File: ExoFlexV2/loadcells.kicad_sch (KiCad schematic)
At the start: 7 parts

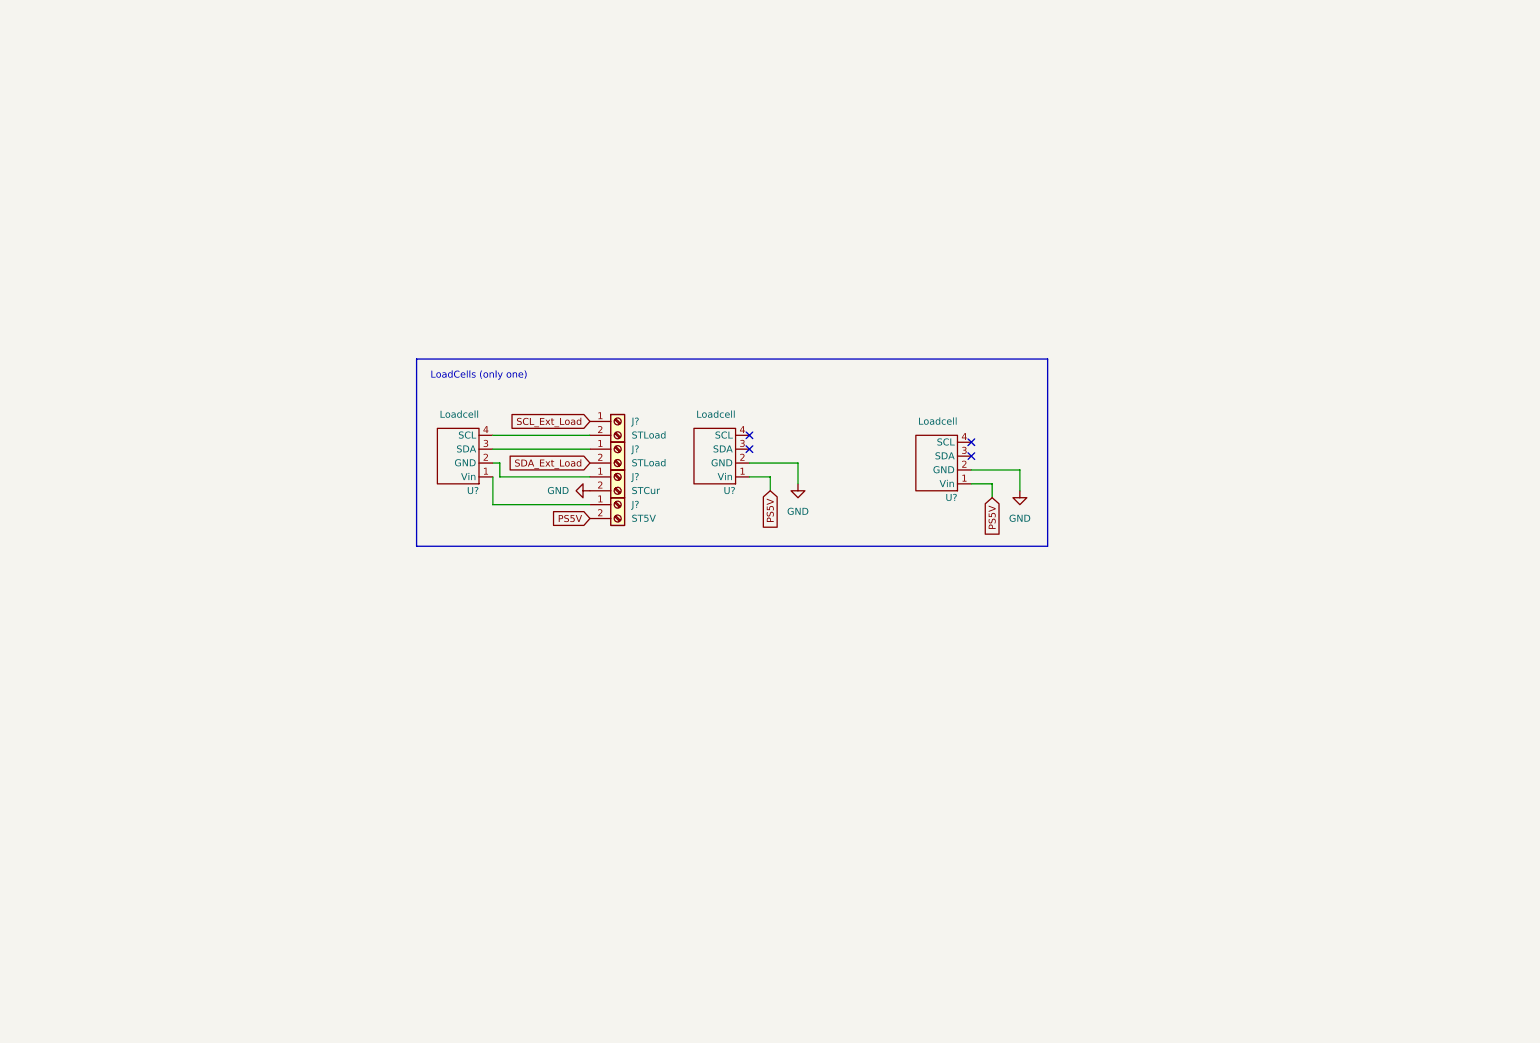
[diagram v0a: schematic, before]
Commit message: Schematic structure
Ajout des Encodeur magnétique et load cells, début de circuit de comparateurs
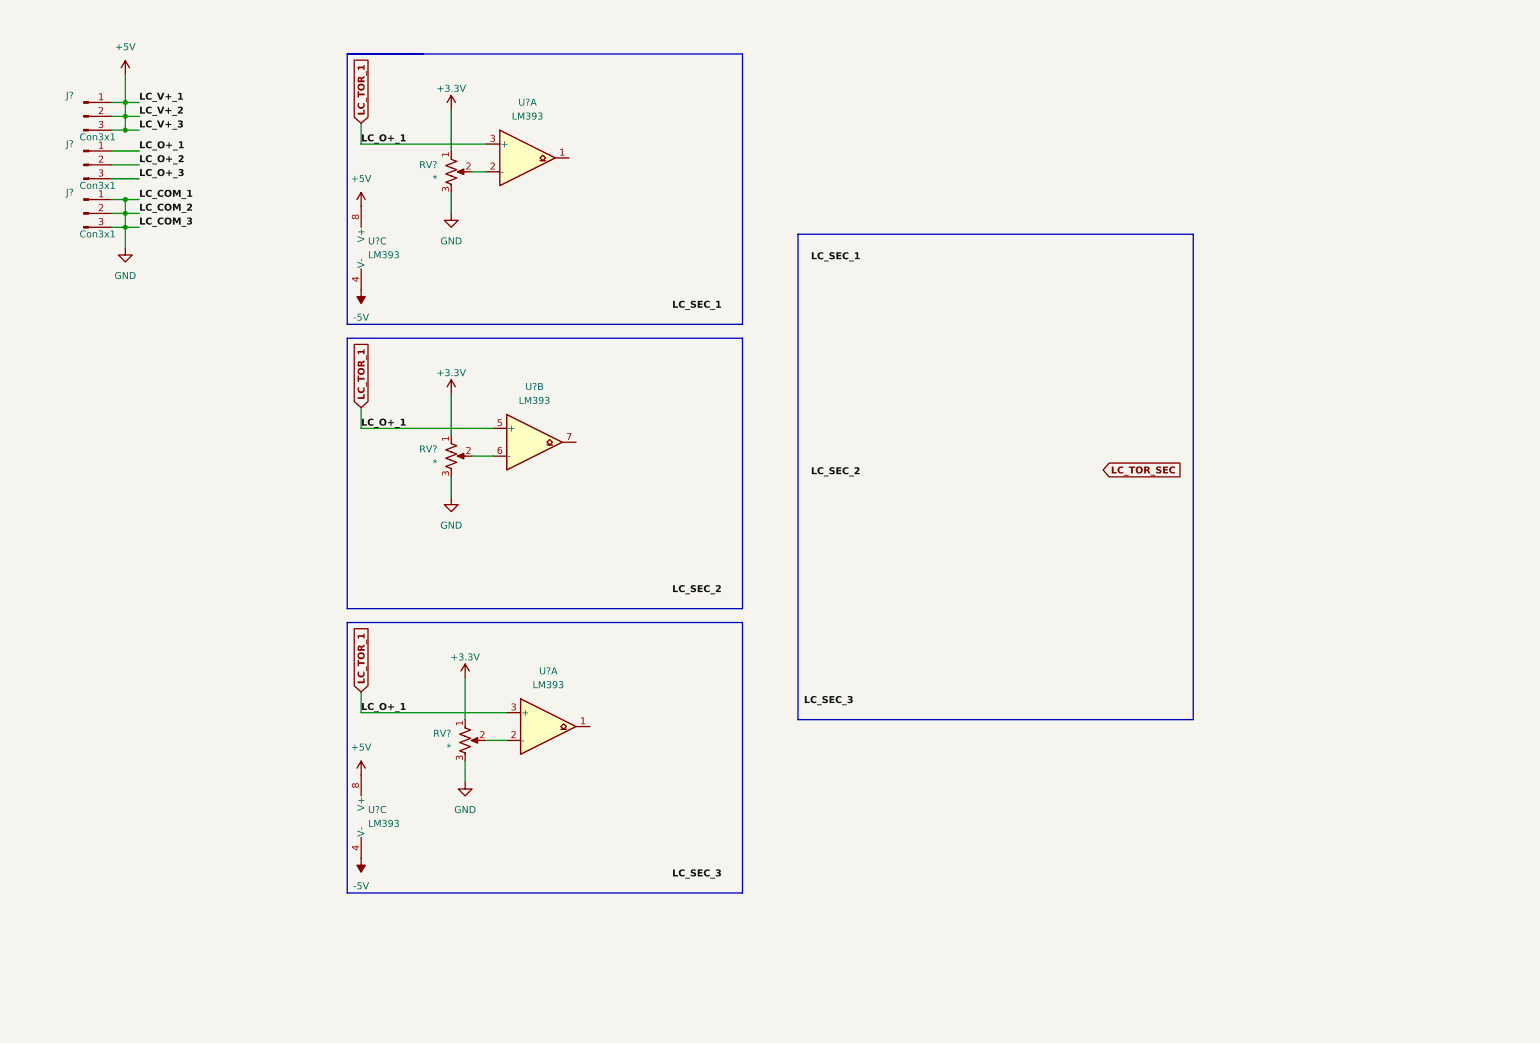
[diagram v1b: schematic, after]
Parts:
- removed J? (x2): STLoad, symbol Connector:Screw_Terminal_01x02
- removed J?: STCur, symbol Connector:Screw_Terminal_01x02
- removed J?: ST5V, symbol Connector:Screw_Terminal_01x02
- removed U? (x3): Loadcell, symbol Sensor_library:MPU6050_acc_gyro
- added J? (x3): Con3x1, symbol Connector:Conn_01x03_Male
- added RV? (x3): *, symbol Device:R_Potentiometer_US
- added U? (x5): LM393, symbol Comparator:LM393
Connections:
- net GND: now also J?.1 (Pin_1), J?.2 (Pin_2), J?.3 (Pin_3), RV?.3, RV?.3, RV?.3
- new net: RV?.2, U?.2 (-) (x2)
- new net: RV?.2, U?.6 (-)
- new net +3.3V: RV?.1, RV?.1, RV?.1
- new net +5V: J?.1 (Pin_1), J?.2 (Pin_2), J?.3 (Pin_3), U?.8 (V+), U?.8 (V+)
- new net -5V: U?.4 (V-), U?.4 (V-)
- new net LC_O+_2: J?.2 (Pin_2)
- new net LC_O+_3: J?.3 (Pin_3)
- new net LC_TOR_1: J?.1 (Pin_1), U?.3 (+), U?.3 (+), U?.5 (+)
- no-connect marks 4 -> 0
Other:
- note removed: "LoadCells (only one)"

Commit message: Many changes
Debouncing, power protection, potentiometer limits, etc.
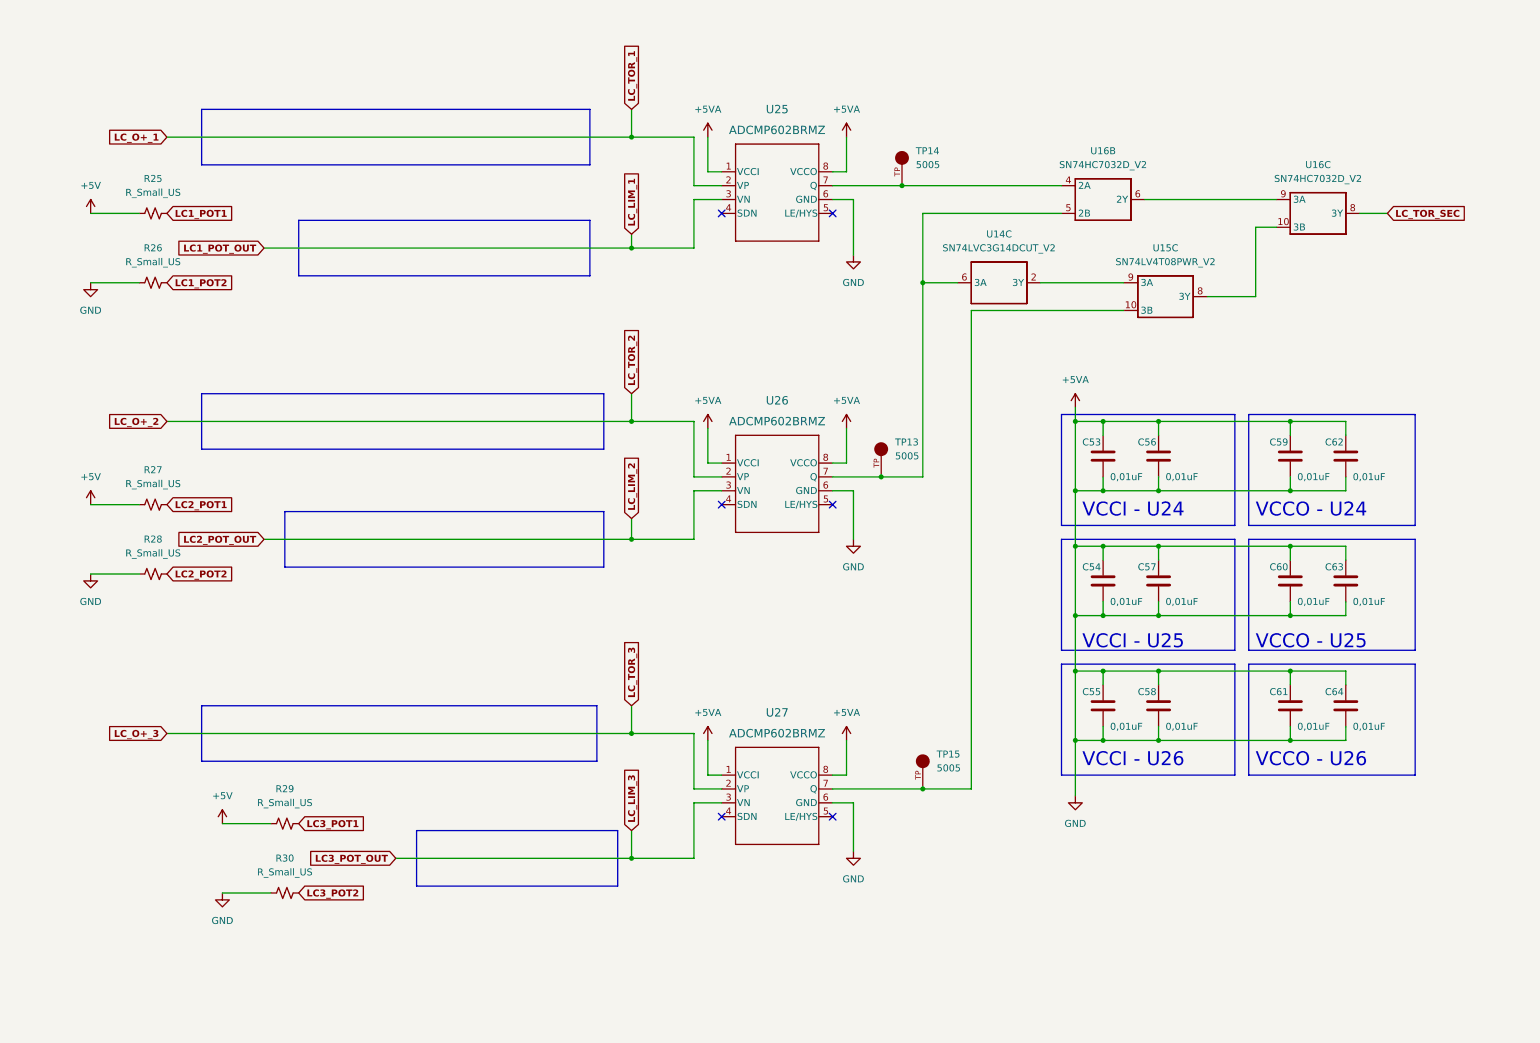
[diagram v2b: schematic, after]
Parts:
- removed J? (x3): Con3x1, symbol Connector:Conn_01x03_Male
- removed RV? (x3): *, symbol Device:R_Potentiometer_US
- removed U? (x5): LM393, symbol Comparator:LM393
- added C53, C54, C55, C56, C57, C58, C59, C60, C61, C62, C63, C64: 0,01uF, Capacitor_SMD:C_0603_1608Metric, symbol Device:C
- added R25, R26, R27, R28, R29, R30: R_Small_US, Resistor_SMD:R_0603_1608Metric, symbol Device:R_Small_US
- added TP13, TP14, TP15: 5005, FootPrint:KEYSTONE_5005, symbol SymLib:5005
- added U14: SN74LVC3G14DCUT_V2, FootPrint:SN74LVC3G14DCUT, symbol SymLib:SN74LVC3G14DCUT_V2
- added U15: SN74LV4T08PWR_V2, FootPrint:SN74LV4T08PWR, symbol SymLib:SN74LV4T08PWR_V2
- added U16: SN74HC7032D_V2, FootPrint:SN74HC7032D, symbol SymLib:SN74HC7032D_V2
- added U25, U26, U27: ADCMP602BRMZ, FootPrint:ADCMP602BRMZ, symbol SymLib:ADCMP602BRMZ
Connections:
- net +5V: now also R25.1, R27.1, R29.1
- net LC_O+_2: now also U26.2 (VP)
- net LC_O+_3: now also U27.2 (VP)
- net LC_TOR_SEC: now also U16.8 (3Y)
- new net: TP13.TP, U14.6 (3A), U16.5 (2B), U26.7 (Q)
- new net: TP15.TP, U15.10 (3B), U27.7 (Q)
- new net: U14.2 (3Y), U15.9 (3A)
- new net: TP14.TP, U16.4 (2A), U25.7 (Q)
- new net: U15.8 (3Y), U16.10 (3B)
- new net: U16.6 (2Y), U16.9 (3A)
- new net +5VA: C53.1, C53.2, C54.1, C54.2, C55.1, C55.2, C56.1, C56.2, C57.1, C57.2, C58.1, C58.2, C59.1, C59.2, C60.1, C60.2, C61.1, C61.2, C62.1, C62.2, C63.1, C63.2, C64.1, C64.2, R26.1, R28.1, R30.1, U25.1 (VCCI), U25.6 (GND), U25.8 (VCCO), U26.1 (VCCI), U26.6 (GND), U26.8 (VCCO), U27.1 (VCCI), U27.6 (GND), U27.8 (VCCO)
- new net LC1_POT1: R25.2
- new net LC1_POT2: R26.2
- new net LC1_POT_OUT: U25.3 (VN)
- new net LC2_POT1: R27.2
- new net LC2_POT2: R28.2
- new net LC2_POT_OUT: U26.3 (VN)
- new net LC3_POT1: R29.2
- new net LC3_POT2: R30.2
- new net LC3_POT_OUT: U27.3 (VN)
- new net LC_O+_1: U25.2 (VP)
- no-connect marks 0 -> 6
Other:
- note added: "VCCI - U24"
- note added: "VCCI - U25"
- note added: "VCCI - U26"
- note added: "VCCO - U24"
- note added: "VCCO - U25"
- note added: "VCCO - U26"

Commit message: quque truc
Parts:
- added C62, C63, C64, C65, C66, C70: 1nF, Capacitor_SMD:C_0603_1608Metric, symbol Device:C
- added C67, C68, C69: 0,1uF, Capacitor_SMD:C_0603_1608Metric, symbol Device:C
- added C71, C72, C73: 1uF, Capacitor_SMD:C_0603_1608Metric, symbol Device:C
- added R42, R43, R46, R47, R48, R52: 7,5k, Resistor_SMD:R_0603_1608Metric, symbol Device:R_Small_US
- added R49, R50, R51: 10k, Resistor_SMD:R_0603_1608Metric, symbol Device:R_Small_US
- added R53, R54, R55: 220k, Resistor_SMD:R_0603_1608Metric, symbol Device:R_Small_US
- added R56, R57, R58, R62, R63, R64: 2M, Resistor_SMD:R_0603_1608Metric, symbol Device:R_Small_US
- added R59, R60, R61: 430k, Resistor_SMD:R_0603_1608Metric, symbol Device:R_Small_US
- added TP32, TP33, TP34, TP35, TP36, TP37, TP41: 5005, FootPrint:KEYSTONE_5005, symbol SymLib:5005
- added U24, U25, U26: MCP6001T-I_OT, FootPrint:SOT95P270X145-5N, symbol SymLib:MCP6001T-I_OT
- renumbered C53 to C74, C54 to C75, C55 to C76, C56 to C77, C57 to C78, C58 to C79, C59 to C80, C60 to C81, C61 to C82, C62 to C83, C63 to C84, C64 to C85, R25 to R38, R26 to R39, R27 to R40, R28 to R41, R29 to R44, R30 to R45, TP13 to TP38, TP14 to TP39, TP15 to TP40, U14 to U15, U15 to U16, U16 to U17, U25 to U27, U26 to U28, U27 to U29
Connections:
- net +5V is gone; now on net +5VA: R38.1, R40.1, R44.1
- net +5VA: now also C67.1, C68.1, C69.1, C71.1, C72.1, C73.1, U24.5, U25.5, U26.5; no longer C74.2, C75.2, C76.2, C77.2, C78.2, C79.2, C80.2, C81.2, C82.2, C83.2, C84.2, C85.2, R39.1, R41.1, R45.1, U27.6 (GND), U28.6 (GND), U29.6 (GND)
- net LC1_POT_OUT: now also R46.1; no longer U27.3 (VN)
- net LC2_POT_OUT: now also R48.1; no longer U28.3 (VN)
- net LC3_POT_OUT: now also R52.1; no longer U29.3 (VN)
- net LC_O+_1: now also R47.1; no longer U27.2 (VP)
- net LC_O+_2: now also R43.1; no longer U28.2 (VP)
- net LC_O+_3: now also R42.1; no longer U29.2 (VP)
- net LC_TOR_SEC: now also TP41.TP
- new net: C64.1, R47.2, U24.3
- new net: R49.2, R53.1, R56.1, U24.4
- new net: R56.2, R59.2, R62.1
- new net: C62.1, R42.2, U26.3
- new net: C63.1, R43.2, U25.3
- new net: R53.2, R59.1
- new net: R51.2, R55.1, R58.1, U26.4
- new net: R58.2, R61.2, R64.1
- new net: R50.2, R54.1, R57.1, U25.4
- new net: R55.2, R61.1
- new net: R54.2, R60.1
- new net: R57.2, R60.2, R63.1
- new net GND: C62.2, C63.2, C64.2, C65.2, C66.2, C67.2, C68.2, C69.2, C70.2, C71.2, C72.2, C73.2, C74.2, C75.2, C76.2, C77.2, C78.2, C79.2, C80.2, C81.2, C82.2, C83.2, C84.2, C85.2, R39.1, R41.1, R45.1, R49.1, R50.1, R51.1, U24.2, U25.2, U26.2, U27.6 (GND), U28.6 (GND), U29.6 (GND)
- new net LC_LIM_1: C65.1, R46.2, TP33.TP, U27.3 (VN)
- new net LC_LIM_2: C66.1, R48.2, TP35.TP, U28.3 (VN)
- new net LC_LIM_3: C70.1, R52.2, TP37.TP, U29.3 (VN)
- new net LC_TOR_1: R62.2, TP32.TP, U24.1, U27.2 (VP)
- new net LC_TOR_2: R63.2, TP34.TP, U25.1, U28.2 (VP)
- new net LC_TOR_3: R64.2, TP36.TP, U26.1, U29.2 (VP)
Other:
- moved on the sheet: R38, R39, R40, R41, R44, R45

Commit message: Placement
Début du placement et modification d'après dernier review
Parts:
- added TP69, TP70, TP71: 5005, FootPrint:KEYSTONE_5005, symbol SymLib:5005
- R37: renamed from R38; value R_Small_US -> 0Ω
- R38: renamed from R39; value R_Small_US -> 0Ω
- R39: renamed from R40; value R_Small_US -> 0Ω
- R40: renamed from R41; value R_Small_US -> 0Ω
- R42: renamed from R44; value R_Small_US -> 0Ω
- R43: renamed from R45; value R_Small_US -> 0Ω
- renumbered C64 to C66, C65 to C67, C63 to C68, C66 to C69, C62 to C70, C67 to C71, C68 to C72, C69 to C73, C71 to C74, C72 to C75, C73 to C76, C70 to C77, C74 to C78, C75 to C79, C76 to C80, C77 to C81, C78 to C82, C79 to C83, C80 to C84, C81 to C85, C82 to C86, C83 to C87, C84 to C88, C85 to C89, R48 to R41, R46 to R44, R43 to R45, R47 to R46, R42 to R47, R49 to R48, R50 to R49, R51 to R50, R53 to R51, R54 to R52, R55 to R53, R56 to R54, R57 to R55, R58 to R56, R59 to R57, R60 to R58, R61 to R59, R52 to R60, R62 to R61, R63 to R62, R64 to R63, TP32 to TP60, TP33 to TP61, TP34 to TP62, TP35 to TP63, TP36 to TP64, TP37 to TP65, TP38 to TP66, TP39 to TP67, TP40 to TP68, TP41 to TP72, U15 to U13, U16 to U15, U17 to U16
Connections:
- net at U13.2 (3Y), U15.9 (3A): now also TP69.TP
- net at U15.8 (3Y), U16.10 (3B): now also TP71.TP
- net at U16.6 (2Y), U16.9 (3A): now also TP70.TP
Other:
- moved on the sheet: C68, C69, C70, C77, R37, R38, R39, R40, R41, R45, R47, R60

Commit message: Placement encore
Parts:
- renumbered C66 to C67, C67 to C68, C68 to C69, C69 to C70, C70 to C71, C71 to C72, C72 to C73, C73 to C74, C74 to C75, C75 to C76, C76 to C77, C77 to C78, C78 to C79, C79 to C80, C80 to C81, C81 to C82, C82 to C83, C83 to C84, C84 to C85, C85 to C86, C86 to C87, C87 to C88, C88 to C89, C89 to C90, R37 to R38, R38 to R39, R39 to R40, R40 to R41, R41 to R42, R42 to R43, R43 to R44, R44 to R45, R45 to R46, R46 to R47, R47 to R48, R48 to R49, R49 to R50, R50 to R51, R51 to R52, R52 to R53, R53 to R54, R54 to R55, R55 to R56, R56 to R57, R57 to R58, R58 to R59, R59 to R60, R60 to R61, R61 to R62, R62 to R63, R63 to R64, U13 to U14, U15 to U16, U16 to U17
